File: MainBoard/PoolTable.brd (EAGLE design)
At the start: 212.1 x 178.3 mm, 41 parts, among them IC6 LM317MBSTT3, M0 MOLEX-ULTRAFIT-1X03VERT, M1 MOLEX-ULTRAFIT-1X03VERT, M2 MOLEX-ULTRAFIT-1X03VERT, M3 MOLEX-ULTRAFIT-1X03VERT, M4 MOLEX-ULTRAFIT-1X03VERT, M5 MOLEX-ULTRAFIT-1X03VERT, M6 MOLEX-ULTRAFIT-1X03VERT, M7 MOLEX-ULTRAFIT-1X03VERT, M8 MOLEX-ULTRAFIT-1X03VERT, U1 TMP102, U2 TMP102, U3 TMP102, U4 TMP102

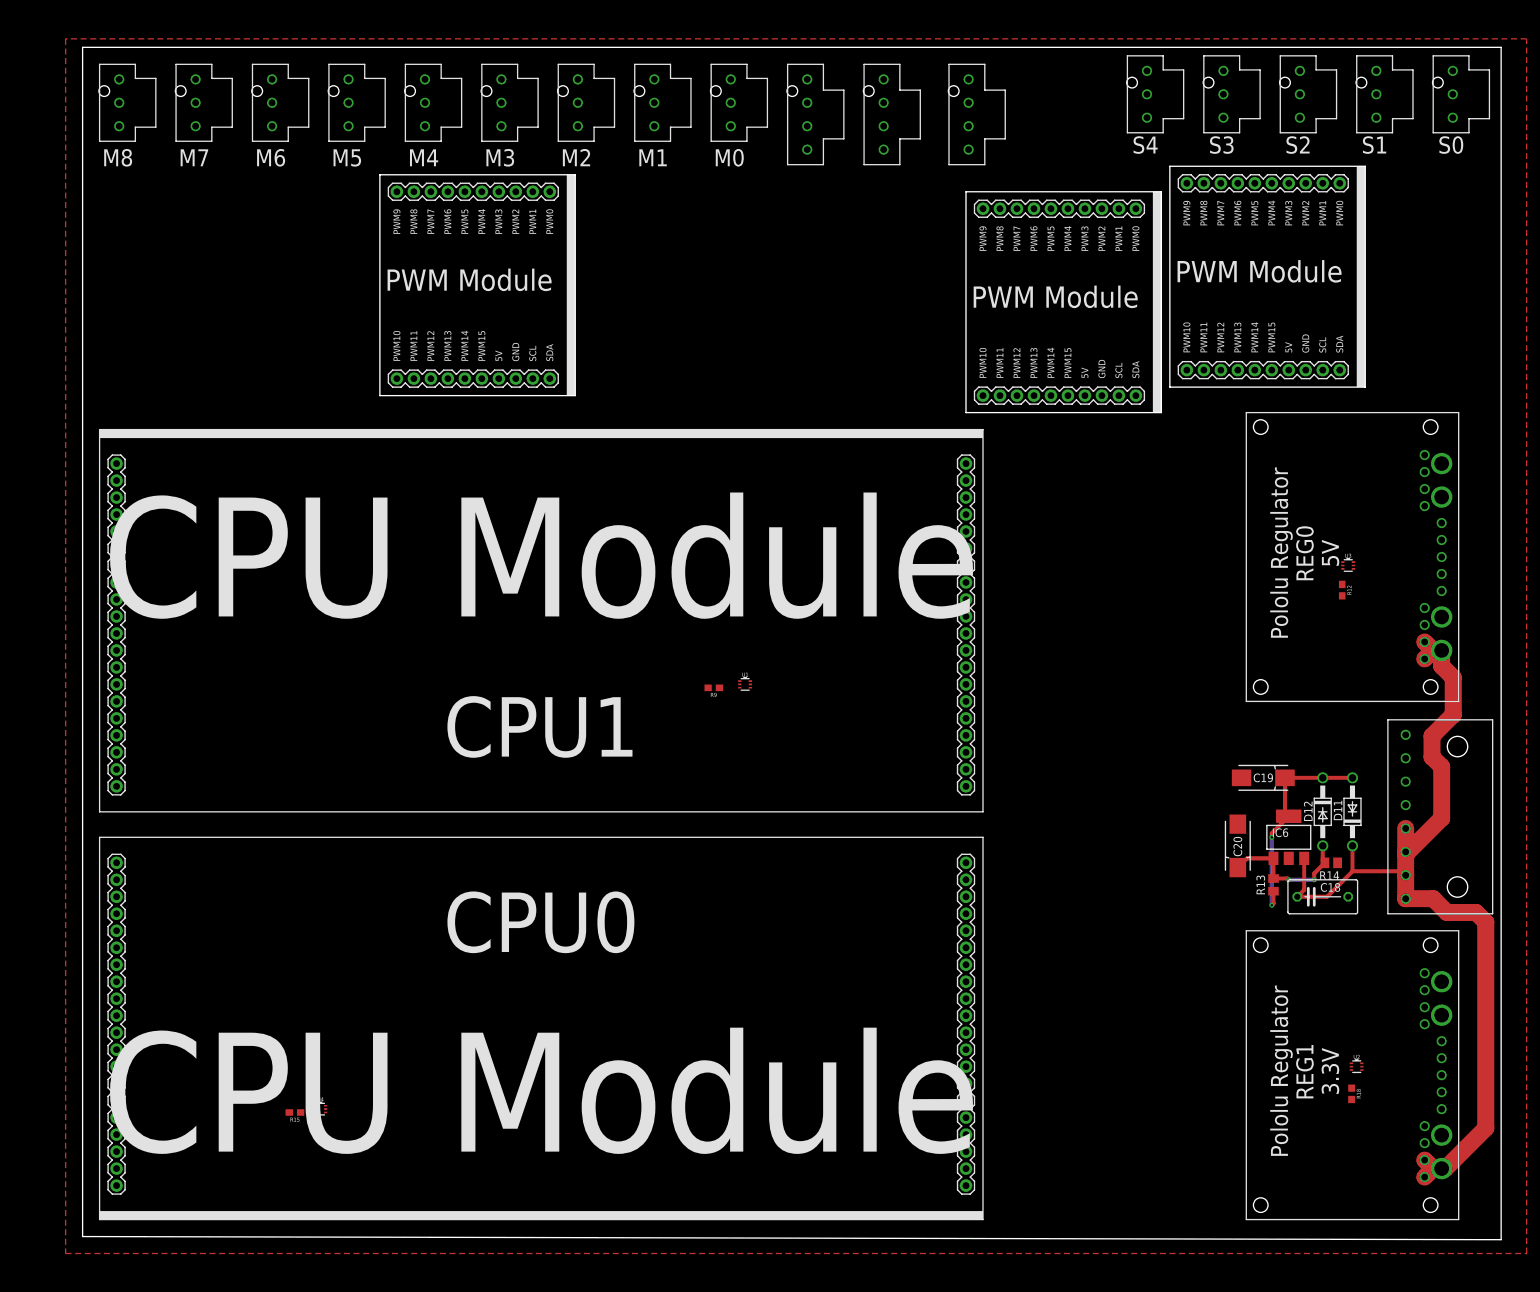
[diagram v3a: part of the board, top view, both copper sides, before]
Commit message: Ultafit library and OSH park rules
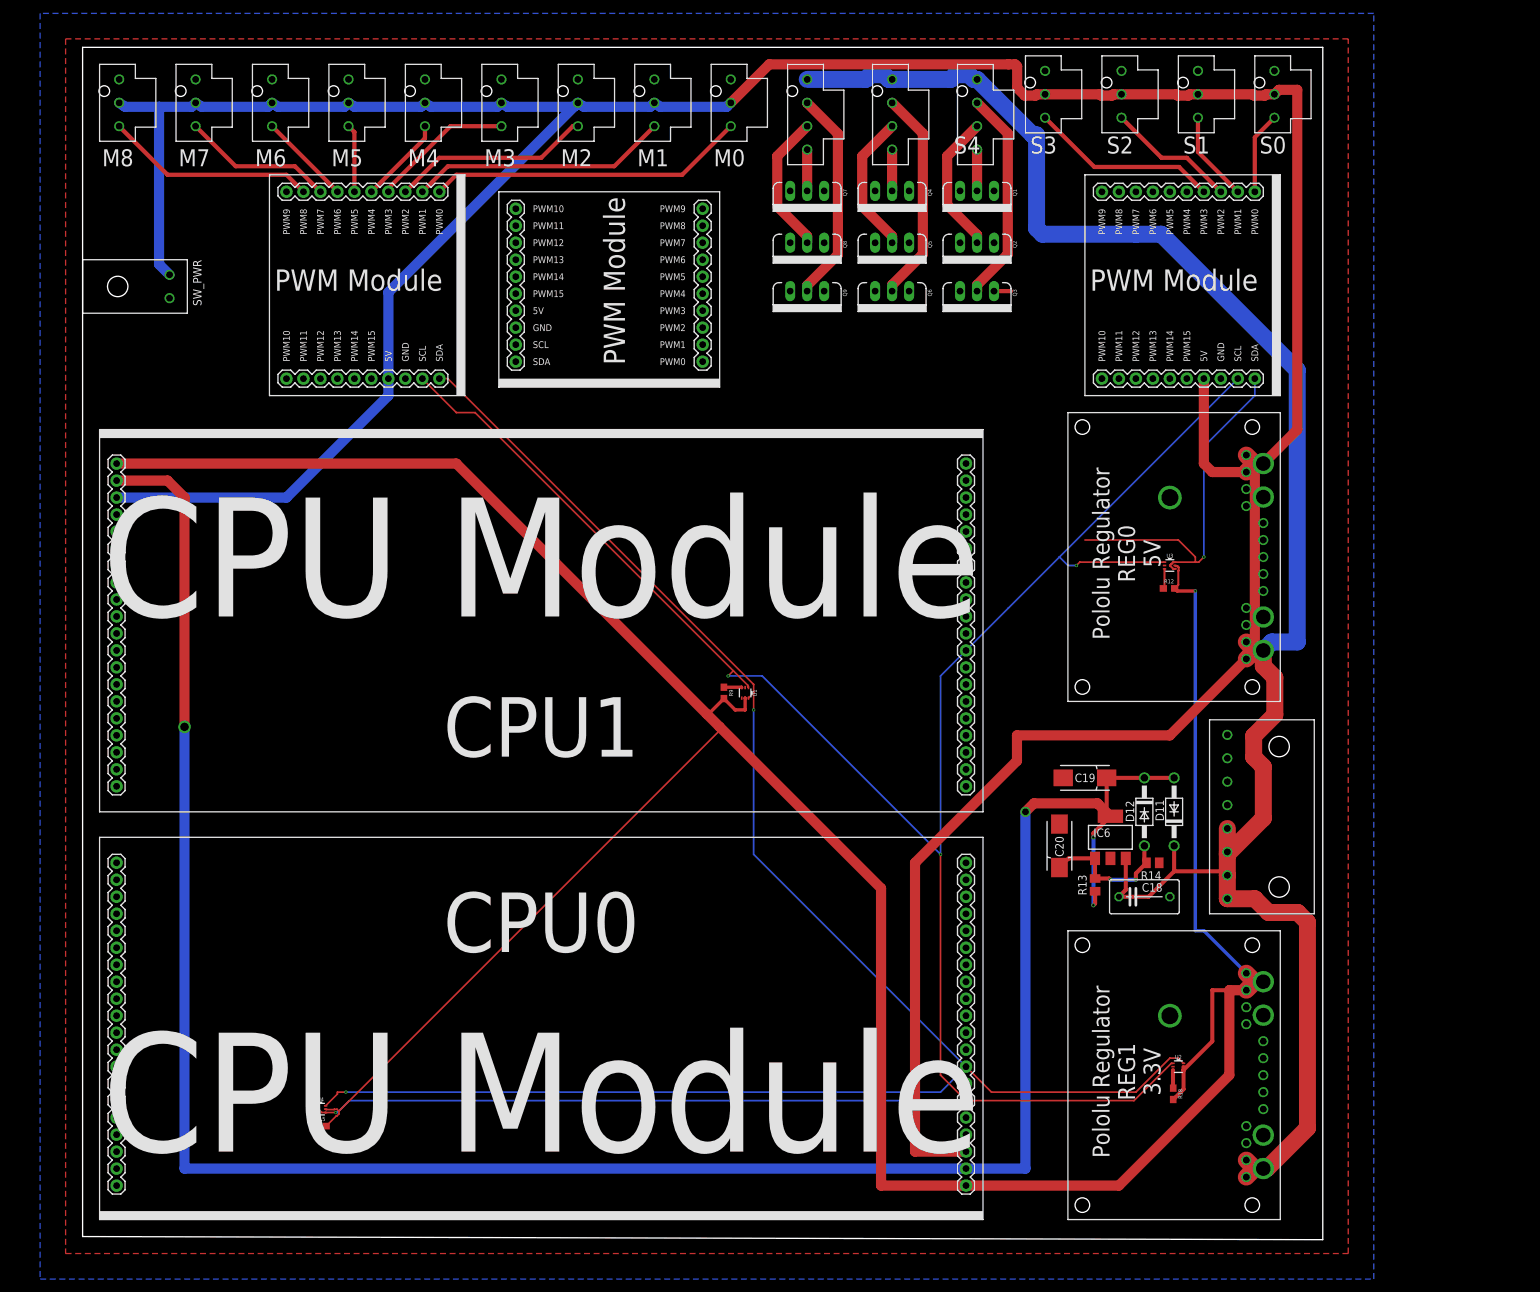
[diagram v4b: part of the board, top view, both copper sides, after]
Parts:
- removed S4: MOLEX-ULTRAFIT-1X03VERT, External:MOLEX-ULTRAFIT-1X03V
- added Q1, Q2, Q3, Q4, Q5, Q6, Q7, Q8, Q9: 60V/32A/35mΩ, SparkFun-DiscreteSemi:TO220V
- added SW_PWR: MOLEX-ULTRAFIT-1X02-HORIZ, MolexUltrafit:MOLEX-ULTRAFIT-1X02H
- M0, M8, S1: value MOLEX-ULTRAFIT-1X03VERT -> MOLEX-ULTRAFIT-1X03-VERT; device External:MOLEX-ULTRAFIT-1X03V -> MolexUltrafit:MOLEX-ULTRAFIT-1X03V
- moved PWM1 36.8 mm to (95.2, 156.2), turned to 180 degrees
- moved D11 26.7 mm to (163.2, 63.5)
- moved IC6 26.7 mm to (153.7, 59.7)
- moved R13 26.7 mm to (151.4, 52.6)
- moved REG0 26.7 mm to (179.1, 80.0)
- moved REG1 26.7 mm to (179.1, 2.54)
- moved S0 26.7 mm to (175.3, 176.5)
- moved C18 26.7 mm to (158.8, 50.8)
- moved C19 26.7 mm to (149.9, 68.6)
- moved C20 26.7 mm to (146.1, 58.4)
- moved D12 26.7 mm to (158.8, 63.5)
- moved PWR_IN 26.7 mm to (184.2, 48.3)
- moved R14 26.7 mm to (160.0, 55.9)
- moved R18 26.7 mm to (163.1, 21.3)
- moved S1 26.7 mm to (163.8, 176.5)
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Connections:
- removed net PWM3_0: PWM1.PWM0
- removed net PWM3_1: PWM1.PWM1
- removed net PWM3_2: PWM1.PWM2
- removed net PWM3_3: PWM1.PWM3
- removed net PWM3_4: PWM1.PWM4
- removed net PWM3_5: PWM1.PWM5
- removed net PWM3_6: PWM1.PWM6
- removed net PWM3_7: PWM1.PWM7
- removed net PWM3_8: PWM1.PWM8
- new net B1: PWM1.PWM2, Q3.1
- new net B2: PWM1.PWM5, Q6.1
- new net B3: PWM1.PWM8, Q9.1
- new net G1: PWM1.PWM1, Q2.1
- new net G2: PWM1.PWM4, Q5.1
- new net G3: PWM1.PWM7, Q8.1
- new net N$1: LED0.P$4, Q1.2
- new net N$10: LED1.P$3, Q5.2
- new net N$11: LED1.P$2, Q6.2
- new net N$13: LED2.P$4, Q7.2
- new net N$14: LED2.P$3, Q8.2
- new net N$16: LED2.P$2, Q9.2
- new net N$2: LED0.P$3, Q2.2
- new net N$3: LED0.P$2, Q3.2
- new net N$8: LED1.P$4, Q4.2
- new net R1: PWM1.PWM0, Q1.1
- new net R2: PWM1.PWM3, Q4.1
- new net R3: PWM1.PWM6, Q7.1
- net 12V: now also LED0.P$1, LED1.P$1, LED2.P$1
- net 5V: now also SW_PWR.P$1; no longer S4.P$2
- net GND: now also Q1.3, Q2.3, Q3.3, Q4.3, Q5.3, Q6.3, Q7.3, Q8.3, Q9.3, SW_PWR.P$2; no longer S4.P$1
- net PWM2_4: no longer S4.P$3
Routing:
- net 5V: track 0.00 -> 541.0 mm
- net 3.3V: track 0.00 -> 449.6 mm, vias 0 -> 1
- net CPU0_SCL0: track 0.00 -> 388.2 mm, vias 0 -> 4
- net CPU0_SDA0: track 0.00 -> 326.9 mm, vias 0 -> 3
- net 1.8V: track 32.6 -> 337.3 mm, vias 2 -> 4
- net 12V: track 136.9 -> 283.8 mm
- net PWM1_0: track 0.00 -> 47.6 mm
- net PWM1_1: track 0.00 -> 38.7 mm
- net N$11: track 0.00 -> 32.0 mm
- net N$3: track 0.00 -> 32.0 mm
- net N$16: track 0.00 -> 32.0 mm
- net PWM1_8: track 0.00 -> 31.6 mm
- net PWM1_2: track 0.00 -> 29.8 mm
- net PWM2_3: track 0.00 -> 28.3 mm
- net PWM1_7: track 0.00 -> 22.7 mm
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- added copper zone on layer 16, net GND
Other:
- board size 212.1 x 178.3 mm -> 185.4 x 178.3 mm

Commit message: latest
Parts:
- added J1, J2: 2X6 FEMALE, SparkFun-Connectors:2X6
- added J3, J4: FEMALE 2x3, SparkFun-Connectors:2X3
- moved SW_PWR 10.2 mm to (0.00, 156.2)
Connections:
- new net N$17: CPU0.39, J3.2, J4.2
- new net N$18: CPU0.40, J3.4, J4.4
- new net N$19: CPU0.38, J3.6, J4.6
- new net N$4: CPU0.12, J1.10, J1.12, J1.2, J1.4, J1.6, J1.8
- new net N$5: CPU0.16, J2.1, J2.11, J2.3, J2.5, J2.7, J2.9
- new net SS1: CPU0.32, J3.3
- new net SS2: CPU0.31, J4.3
- net 5V: now also J1.1, J1.11, J1.3, J1.5, J1.7, J1.9, J3.1, J4.1
- net GND: now also J2.10, J2.12, J2.2, J2.4, J2.6, J2.8, J3.5, J4.5
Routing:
- net 5V: track 541.0 -> 530.8 mm
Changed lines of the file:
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@@
 <attribute name="PROD_ID" value="TRANS-10060" x="108.331" y="141.351" size="2.54" layer="27" rot="R180" display="off"/>
 </element>
-<element name="SW_PWR" library="MolexUltrafit" package="MOLEX-ULTRAFIT-1X02H" value="MOLEX-ULTRAFIT-1X02-HORIZ" x="0" y="146.05" smashed="yes" rot="R270">
-<attribute name="NAME" x="16.51" y="146.05" size="1.27" layer="21" rot="R270"/>
+<element name="SW_PWR" library="MolexUltrafit" package="MOLEX-ULTRAFIT-1X02H" value="MOLEX-ULTRAFIT-1X02-HORIZ" x="0" y="156.21" smashed="yes" rot="R270">
+<attribute name="NAME" x="16.51" y="156.21" size="1.27" layer="21" rot="R270"/>
+</element>
+<element name="J1" library="SparkFun-Connectors" package="2X6" value="2X6 FEMALE" x="11.43" y="132.08" smashed="yes" rot="R90">
+<attribute name="PROD_ID" value="CONN-12423" x="11.43" y="132.08" size="1.778" layer="27" rot="R90" display="off"/>
+</element>
+<element name="J2" library="SparkFun-Connectors" package="2X6" value="2X6 FEMALE" x="6.35" y="132.08" smashed="yes" rot="R90">
+<attribute name="PROD_ID" value="CONN-12423" x="6.35" y="132.08" size="1.778" layer="27" rot="R90" display="off"/>
+</element>
+<element name="J3" library="SparkFun-Connectors" package="2X3" value="FEMALE 2x3" x="3.81" y="124.46" smashed="yes">
+<attribute name="NAME" x="2.54" y="128.524" size="0.6096" layer="25" font="vector" ratio="20"/>
+<attribute name="PROD_ID" value="CONN-11566" x="3.81" y="124.46" size="1.778" layer="27" display="off"/>
+<attribute name="VALUE" x="2.54" y="122.047" size="0.6096" layer="27" font="vector" ratio="20"/>
+</element>
+<element name="J4" library="SparkFun-Connectors" package="2X3" value="FEMALE 2x3" x="13.97" y="124.46" smashed="yes">
+<attribute name="NAME" x="12.7" y="128.524" size="0.6096" layer="25" font="vector" ratio="20"/>
+<attribute name="PROD_ID" value="CONN-11566" x="13.97" y="124.46" size="1.778" layer="27" display="off"/>
+<attribute name="VALUE" x="12.7" y="122.047" size="0.6096" layer="27" font="vector" ratio="20"/>
 </element>
 </elements>
@@
 <via x="162.56" y="110.49" extent="1-16" drill="2.54"/>
 <contactref element="SW_PWR" pad="P$2"/>
+<contactref element="J2" pad="2"/>
+<contactref element="J2" pad="12"/>
+<contactref element="J2" pad="10"/>
+<contactref element="J2" pad="8"/>
+<contactref element="J2" pad="6"/>
+<contactref element="J2" pad="4"/>
+<contactref element="J3" pad="5"/>
+<contactref element="J4" pad="5"/>
 <wire x1="105.791" y1="141.351" x2="105.791" y2="148.59" width="0" layer="19" extent="1-1"/>
 <wire x1="105.791" y1="156.337" x2="105.791" y2="148.59" width="0" layer="19" extent="1-1"/>
@@
 <wire x1="166.76" y1="174.28" x2="155.33" y2="174.28" width="0" layer="19" extent="1-1"/>
 <wire x1="178.19" y1="174.28" x2="166.76" y2="174.28" width="0" layer="19" extent="1-1"/>
-<wire x1="13" y1="140.3" x2="16.9" y2="173.01" width="0" layer="19" extent="1-1"/>
-<wire x1="5.08" y1="107.95" x2="13" y2="140.3" width="0" layer="19" extent="1-1"/>
+<wire x1="13" y1="150.46" x2="16.9" y2="173.01" width="0" layer="19" extent="1-1"/>
+<wire x1="132.08" y1="107.95" x2="131.191" y2="141.351" width="0" layer="19" extent="1-1"/>
 <wire x1="132.08" y1="55.88" x2="132.08" y2="67.31" width="0" layer="19" extent="1-1"/>
 <wire x1="146.61" y1="68.58" x2="132.08" y2="67.31" width="0" layer="19" extent="1-1"/>
@@
 <wire x1="99.063303125" y1="82.08" x2="132.08" y2="82.55" width="0" layer="19" extent="1-1"/>
 <wire x1="98.554159375" y1="80.503584375" x2="99.063303125" y2="82.08" width="0" layer="19" extent="1-1"/>
+<wire x1="3.81" y1="139.7" x2="5.08" y2="15.24" width="0" layer="19" extent="1-1"/>
+<wire x1="3.81" y1="137.16" x2="3.81" y2="139.7" width="0" layer="19" extent="1-1"/>
+<wire x1="3.81" y1="134.62" x2="3.81" y2="137.16" width="0" layer="19" extent="1-1"/>
+<wire x1="3.81" y1="132.08" x2="3.81" y2="134.62" width="0" layer="19" extent="1-1"/>
+<wire x1="3.81" y1="142.24" x2="3.81" y2="139.7" width="0" layer="19" extent="1-1"/>
+<wire x1="3.81" y1="144.78" x2="3.81" y2="142.24" width="0" layer="19" extent="1-1"/>
+<wire x1="8.89" y1="124.46" x2="3.81" y2="137.16" width="0" layer="19" extent="1-1"/>
+<wire x1="19.05" y1="124.46" x2="8.89" y2="124.46" width="0" layer="19" extent="1-1"/>
 <wire x1="64.77" y1="135.89" x2="62.62" y2="173.01" width="0" layer="19" extent="1-1"/>
 <wire x1="48.26" y1="128.27" x2="64.77" y2="135.89" width="0" layer="19" extent="1-1"/>
@@
 <wire x1="102.66" y1="175.26" x2="96.91" y2="169.51" width="1.524" layer="1"/>
 <contactref element="SW_PWR" pad="P$1"/>
-<wire x1="138.43" y1="175.26" x2="102.66" y2="175.26" width="1.524" layer="1"/>
-<wire x1="11.43" y1="168.91" x2="11.43" y2="145.37" width="1.524" layer="16"/>
-<wire x1="11.43" y1="145.37" x2="13" y2="143.8" width="1.524" layer="16"/>
-<wire x1="139.42" y1="175.26" x2="138.43" y2="175.26" width="1.524" layer="1"/>
+<wire x1="139.42" y1="175.26" x2="102.66" y2="175.26" width="1.524" layer="1"/>
+<wire x1="11.43" y1="168.91" x2="11.43" y2="155.53" width="1.524" layer="16"/>
+<wire x1="11.43" y1="155.53" x2="13" y2="153.96" width="1.524" layer="16"/>
 <wire x1="142.47481875" y1="170.587" x2="140.86518125" y2="170.587" width="1.524" layer="1"/>
 <wire x1="140.86518125" y1="170.587" x2="139.727" y2="171.72518125" width="1.524" layer="1"/>
@@
 <wire x1="139.727" y1="174.953" x2="139.42" y2="175.26" width="1.524" layer="1"/>
 <wire x1="139.727" y1="171.72518125" x2="139.727" y2="174.953" width="1.524" layer="1"/>
+<contactref element="J1" pad="1"/>
+<contactref element="J1" pad="11"/>
+<contactref element="J1" pad="9"/>
+<contactref element="J1" pad="7"/>
+<contactref element="J1" pad="5"/>
+<contactref element="J1" pad="3"/>
+<contactref element="J3" pad="1"/>
+<contactref element="J4" pad="1"/>
 <wire x1="45.72" y1="141.18" x2="64.77" y2="138.43" width="0" layer="19" extent="16-16"/>
 <wire x1="175.26" y1="114.3" x2="173.99" y2="114.3" width="0" layer="19" extent="1-1"/>
+<wire x1="11.43" y1="144.78" x2="124.46" y2="12.7" width="0" layer="19" extent="1-1"/>
+<wire x1="11.43" y1="142.24" x2="11.43" y2="144.78" width="0" layer="19" extent="1-1"/>
+<wire x1="11.43" y1="139.7" x2="11.43" y2="142.24" width="0" layer="19" extent="1-1"/>
+<wire x1="11.43" y1="137.16" x2="11.43" y2="139.7" width="0" layer="19" extent="1-1"/>
+<wire x1="11.43" y1="134.62" x2="11.43" y2="137.16" width="0" layer="19" extent="1-1"/>
+<wire x1="11.43" y1="132.08" x2="11.43" y2="134.62" width="0" layer="19" extent="1-1"/>
+<wire x1="3.81" y1="124.46" x2="11.43" y2="132.08" width="0" layer="19" extent="1-1"/>
+<wire x1="13.97" y1="124.46" x2="3.81" y2="124.46" width="0" layer="19" extent="1-1"/>
 </signal>
 <signal name="3.3V">
@@
 <wire x1="92.71" y1="151.13" x2="110.871" y2="141.351" width="0" layer="19" extent="1-1"/>
 </signal>
+<signal name="N$4">
+<contactref element="CPU0" pad="12"/>
+<contactref element="J1" pad="12"/>
+<contactref element="J1" pad="10"/>
+<contactref element="J1" pad="8"/>
+<contactref element="J1" pad="6"/>
+<contactref element="J1" pad="4"/>
+<contactref element="J1" pad="2"/>
+<wire x1="8.89" y1="144.78" x2="132.08" y2="27.94" width="0" layer="19" extent="1-1"/>
+<wire x1="8.89" y1="142.24" x2="8.89" y2="144.78" width="0" layer="19" extent="1-1"/>
+<wire x1="8.89" y1="139.7" x2="8.89" y2="142.24" width="0" layer="19" extent="1-1"/>
+<wire x1="8.89" y1="137.16" x2="8.89" y2="139.7" width="0" layer="19" extent="1-1"/>
+<wire x1="8.89" y1="134.62" x2="8.89" y2="137.16" width="0" layer="19" extent="1-1"/>
+<wire x1="8.89" y1="132.08" x2="8.89" y2="134.62" width="0" layer="19" extent="1-1"/>
+</signal>
+<signal name="N$5">
+<contactref element="J2" pad="11"/>
+<contactref element="CPU0" pad="16"/>
+<contactref element="J2" pad="9"/>
+<contactref element="J2" pad="7"/>
+<contactref element="J2" pad="5"/>
+<contactref element="J2" pad="3"/>
+<contactref element="J2" pad="1"/>
+<wire x1="6.35" y1="144.78" x2="132.08" y2="17.78" width="0" layer="19" extent="1-1"/>
+<wire x1="6.35" y1="142.24" x2="6.35" y2="144.78" width="0" layer="19" extent="1-1"/>
+<wire x1="6.35" y1="139.7" x2="6.35" y2="142.24" width="0" layer="19" extent="1-1"/>
+<wire x1="6.35" y1="137.16" x2="6.35" y2="139.7" width="0" layer="19" extent="1-1"/>
+<wire x1="6.35" y1="134.62" x2="6.35" y2="137.16" width="0" layer="19" extent="1-1"/>
+<wire x1="6.35" y1="132.08" x2="6.35" y2="134.62" width="0" layer="19" extent="1-1"/>
+</signal>
+<signal name="N$17">
+<contactref element="CPU0" pad="39"/>
+<contactref element="J3" pad="2"/>
+<contactref element="J4" pad="2"/>
+<wire x1="3.81" y1="127" x2="13.97" y2="127" width="0" layer="19" extent="1-1"/>
+<wire x1="5.08" y1="10.16" x2="3.81" y2="127" width="0" layer="19" extent="1-1"/>
+</signal>
+<signal name="N$18">
+<contactref element="CPU0" pad="40"/>
+<contactref element="J3" pad="4"/>
+<contactref element="J4" pad="4"/>
+<wire x1="6.35" y1="127" x2="16.51" y2="127" width="0" layer="19" extent="1-1"/>
+<wire x1="5.08" y1="7.62" x2="6.35" y2="127" width="0" layer="19" extent="1-1"/>
+</signal>
+<signal name="N$19">
+<contactref element="CPU0" pad="38"/>
+<contactref element="J3" pad="6"/>
+<contactref element="J4" pad="6"/>
+<wire x1="8.89" y1="127" x2="19.05" y2="127" width="0" layer="19" extent="1-1"/>
+<wire x1="5.08" y1="12.7" x2="8.89" y2="127" width="0" layer="19" extent="1-1"/>
+</signal>
+<signal name="SS1">
+<contactref element="CPU0" pad="32"/>
+<contactref element="J3" pad="3"/>
+<wire x1="6.35" y1="124.46" x2="5.08" y2="27.94" width="0" layer="19" extent="1-1"/>
+</signal>
+<signal name="SS2">
+<contactref element="CPU0" pad="31"/>
+<contactref element="J4" pad="3"/>
+<wire x1="5.08" y1="30.48" x2="16.51" y2="124.46" width="0" layer="19" extent="1-1"/>
+</signal>
 </signals>
